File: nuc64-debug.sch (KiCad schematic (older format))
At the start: 5 parts, among them J1 SWD

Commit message: First draft for 0.2.x
Uart TX/RX have been swapped
Buttons for Reset/Boot0 have been added
Pinheader for power pins has been added
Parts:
- removed GND1, VDD1: Conn_01x01_Male, Connector_PinHeader_2.54mm:PinHeader_1x01_P2.54mm_Vertical, symbol Connector:Conn_01x01_Male
- added C1: 100n, Capacitor_SMD:C_0603_1608Metric, symbol Device:C
- added J2: POW, Connector_PinHeader_2.54mm:PinHeader_1x03_P2.54mm_Vertical, symbol Connector:Conn_01x03_Female
- added R1: 330, Resistor_SMD:R_0603_1608Metric, symbol Device:R
- added SW1: BOOT, footprints:panasonic_evpa302k, symbol Switch:SW_DIP_x01
- added SW2: RST, footprints:panasonic_evpa302k, symbol Switch:SW_DIP_x01
- DBG1: value Conn_01x10_Female -> DBG
- UART1: value Conn_01x02_Male -> UART
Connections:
- wire segments 18 -> 36
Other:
- note added: "1: ->VDD 3V3 Target\n2 :SWCLK\n3: GND\n4: SWDIO\n5: NRST\n6: SWO(reserved)\n7: Uart TX\n8: Uart RX\n9: VIN 5V\n10: BOOT0/reserved\n\nSTM32F303 does not support USB\nUse STM32F103C8 like onboard flashers\n"
- note added: "The boot-pin might be hard routed to ground.\n330 Ohms will limit current to 10mA @3V3."
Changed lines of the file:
@@
 EESchema Schematic File Version 4
-LIBS:stdebug-cache
-EELAYER 26 0
+EELAYER 30 0
 EELAYER END
 $Descr A4 11693 8268
@@
 P 4700 2600
 F 0 "DBG1" H 4594 3185 50  0000 C CNN
-F 1 "Conn_01x10_Female" H 4594 3094 50  0000 C CNN
+F 1 "DBG" H 4594 3094 50  0000 C CNN
 F 2 "footprints:Hirose_FH12-10S-0.5SH_1x10_P0.5mm_Horizontal" H 4700 2600 50  0001 C CNN
 F 3 "~" H 4700 2600 50  0001 C CNN
@@
 $EndComp
 Wire Wire Line
-	4900 2200 5700 2200
-Wire Wire Line
 	4900 2300 6800 2300
 Wire Wire Line
@@
 	6800 2500 4900 2500
 Wire Wire Line
-	4900 2600 6800 2600
+	4900 2600 5900 2600
 Wire Wire Line
 	4900 2700 6800 2700
@@
 P 6800 3200
 F 0 "UART1" H 6773 3173 50  0000 R CNN
-F 1 "Conn_01x02_Male" H 6773 3082 50  0000 R CNN
+F 1 "UART" H 6773 3082 50  0000 R CNN
 F 2 "Connector_PinSocket_2.54mm:PinSocket_1x02_P2.54mm_Vertical" H 6800 3200 50  0001 C CNN
 F 3 "~" H 6800 3200 50  0001 C CNN
@@
 	4900 2800 6300 2800
 Wire Wire Line
-	6300 2800 6300 3200
-Wire Wire Line
-	6300 3200 6600 3200
-Wire Wire Line
 	4900 2900 6100 2900
-Wire Wire Line
-	6100 2900 6100 3300
-Wire Wire Line
-	6100 3300 6600 3300
-$Comp
-L Connector:Conn_01x01_Male VDD1
-U 1 1 5BB98E93
-P 5500 2000
-F 0 "VDD1" H 5606 2178 50  0000 C CNN
-F 1 "Conn_01x01_Male" H 5606 2087 50  0000 C CNN
-F 2 "Connector_PinHeader_2.54mm:PinHeader_1x01_P2.54mm_Vertical" H 5500 2000 50  0001 C CNN
-F 3 "~" H 5500 2000 50  0001 C CNN
-	1    5500 2000
-	1    0    0    -1
-$EndComp
-$Comp
-L Connector:Conn_01x01_Male GND1
-U 1 1 5BB99075
-P 6100 2000
-F 0 "GND1" H 6206 2178 50  0000 C CNN
-F 1 "Conn_01x01_Male" H 6206 2087 50  0000 C CNN
-F 2 "Connector_PinHeader_2.54mm:PinHeader_1x01_P2.54mm_Vertical" H 6100 2000 50  0001 C CNN
-F 3 "~" H 6100 2000 50  0001 C CNN
-	1    6100 2000
-	1    0    0    -1
-$EndComp
-Wire Wire Line
-	5700 2000 5700 2200
-Connection ~ 5700 2200
-Wire Wire Line
-	5700 2200 6800 2200
-Wire Wire Line
-	6300 2000 6300 2400
-Connection ~ 6300 2400
-Wire Wire Line
-	6300 2400 6800 2400
 $Comp
 L power:GND #PWR0101
@@
 	5450 2400 5450 3300
 Connection ~ 5450 2400
-Wire Wire Line
-	5450 2400 6300 2400
+$Comp
+L Switch:SW_DIP_x01 SW2
+U 1 1 60F10269
+P 5900 4000
+F 0 "SW2" V 5854 4130 50  0000 L CNN
+F 1 "RST" V 5945 4130 50  0000 L CNN
+F 2 "footprints:panasonic_evpa302k" H 5900 4000 50  0001 C CNN
+F 3 "~" H 5900 4000 50  0001 C CNN
+	1    5900 4000
+	0    1    1    0
+$EndComp
+$Comp
+L power:GND #PWR0102
+U 1 1 60F10CF3
+P 5900 4600
+F 0 "#PWR0102" H 5900 4350 50  0001 C CNN
+F 1 "GND" H 5905 4427 50  0000 C CNN
+F 2 "" H 5900 4600 50  0001 C CNN
+F 3 "" H 5900 4600 50  0001 C CNN
+	1    5900 4600
+	1    0    0    -1
+$EndComp
+Wire Wire Line
+	5900 2600 5900 3600
+Connection ~ 5900 2600
+Wire Wire Line
+	5900 2600 6800 2600
+Wire Wire Line
+	5900 4300 5900 4400
+Wire Wire Line
+	6100 2900 6100 3200
+Wire Wire Line
+	6600 3200 6100 3200
+Wire Wire Line
+	6300 2800 6300 3300
+Wire Wire Line
+	6300 3300 6600 3300
+Text Notes 2900 3000 0    50   ~ 0
+1: ->VDD 3V3 Target\n2 :SWCLK\n3: GND\n4: SWDIO\n5: NRST\n6: SWO(reserved)\n7: Uart TX\n8: Uart RX\n9: VIN 5V\n10: BOOT0/reserved\n\nSTM32F303 does not support USB\nUse STM32F103C8 like onboard flashers\n
+$Comp
+L Switch:SW_DIP_x01 SW1
+U 1 1 60F178B4
+P 5100 4100
+F 0 "SW1" V 5054 4230 50  0000 L CNN
+F 1 "BOOT" V 5145 4230 50  0000 L CNN
+F 2 "footprints:panasonic_evpa302k" H 5100 4100 50  0001 C CNN
+F 3 "~" H 5100 4100 50  0001 C CNN
+	1    5100 4100
+	0    1    1    0
+$EndComp
+$Comp
+L power:GND #PWR0103
+U 1 1 60F178D0
+P 5100 4600
+F 0 "#PWR0103" H 5100 4350 50  0001 C CNN
+F 1 "GND" H 5105 4427 50  0000 C CNN
+F 2 "" H 5100 4600 50  0001 C CNN
+F 3 "" H 5100 4600 50  0001 C CNN
+	1    5100 4600
+	1    0    0    -1
+$EndComp
+$Comp
+L Device:R R1
+U 1 1 60F18930
+P 5100 3550
+F 0 "R1" H 5170 3596 50  0000 L CNN
+F 1 "330" H 5170 3505 50  0000 L CNN
+F 2 "Resistor_SMD:R_0603_1608Metric" V 5030 3550 50  0001 C CNN
+F 3 "~" H 5100 3550 50  0001 C CNN
+	1    5100 3550
+	1    0    0    -1
+$EndComp
+Wire Wire Line
+	4900 3100 5100 3100
+Wire Wire Line
+	5100 3100 5100 3400
+Wire Wire Line
+	5100 3700 5100 3800
+Wire Wire Line
+	5100 4600 5100 4400
+Text Notes 3150 3650 0    50   ~ 0
+The boot-pin might be hard routed to ground.\n330 Ohms will limit current to 10mA @3V3.
+$Comp
+L Connector:Conn_01x03_Female J2
+U 1 1 60F1E01B
+P 5000 1500
+F 0 "J2" H 4892 1175 50  0000 C CNN
+F 1 "POW" H 4892 1266 50  0000 C CNN
+F 2 "Connector_PinHeader_2.54mm:PinHeader_1x03_P2.54mm_Vertical" H 5000 1500 50  0001 C CNN
+F 3 "~" H 5000 1500 50  0001 C CNN
+	1    5000 1500
+	-1   0    0    1
+$EndComp
+Wire Wire Line
+	4900 2200 5750 2200
+Wire Wire Line
+	5450 2400 5600 2400
+Wire Wire Line
+	5200 1600 5600 1600
+Wire Wire Line
+	5600 1600 5600 2400
+Connection ~ 5600 2400
+Wire Wire Line
+	5600 2400 6800 2400
+Wire Wire Line
+	5200 1500 5750 1500
+Wire Wire Line
+	5750 1500 5750 2200
+Connection ~ 5750 2200
+Wire Wire Line
+	5750 2200 6800 2200
+Wire Wire Line
+	5200 1400 6000 1400
+Wire Wire Line
+	6000 1400 6000 3000
+Wire Wire Line
+	6000 3000 4900 3000
+$Comp
+L Device:C C1
+U 1 1 60F2F8B5
+P 6500 4000
+F 0 "C1" H 6615 4046 50  0000 L CNN
+F 1 "100n" H 6615 3955 50  0000 L CNN
+F 2 "Capacitor_SMD:C_0603_1608Metric" H 6538 3850 50  0001 C CNN
+F 3 "~" H 6500 4000 50  0001 C CNN
+	1    6500 4000
+	1    0    0    -1
+$EndComp
+Wire Wire Line
+	6500 3850 6500 3600
+Wire Wire Line
+	6500 3600 5900 3600
+Connection ~ 5900 3600
+Wire Wire Line
+	5900 3600 5900 3700
+Wire Wire Line
+	6500 4150 6500 4400
+Wire Wire Line
+	6500 4400 5900 4400
+Connection ~ 5900 4400
+Wire Wire Line
+	5900 4400 5900 4600
 $EndSCHEMATC

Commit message: shrink
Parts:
- added D1: LED, LED_SMD:LED_0603_1608Metric, symbol Device:LED
- added R2: R, Resistor_SMD:R_0603_1608Metric, symbol Device:R
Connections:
- net GND: now also R2.2
- net VDD: now also D1.2 (A)
- new net: D1.1 (K), R2.1
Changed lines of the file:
@@
 Connection ~ 5750 2200
 Wire Wire Line
-	5750 2200 6800 2200
+	5750 2200 6400 2200
 Wire Wire Line
 	5200 1400 6000 1400
@@
 Wire Wire Line
 	5900 4400 5900 4600
+$Comp
+L power:GND #PWR0104
+U 1 1 60F4062E
+P 8150 3650
+F 0 "#PWR0104" H 8150 3400 50  0001 C CNN
+F 1 "GND" H 8155 3477 50  0000 C CNN
+F 2 "" H 8150 3650 50  0001 C CNN
+F 3 "" H 8150 3650 50  0001 C CNN
+	1    8150 3650
+	1    0    0    -1
+$EndComp
+$Comp
+L Device:R R2
+U 1 1 60F4083F
+P 8150 3350
+F 0 "R2" H 8220 3396 50  0000 L CNN
+F 1 "R" H 8220 3305 50  0000 L CNN
+F 2 "Resistor_SMD:R_0603_1608Metric" V 8080 3350 50  0001 C CNN
+F 3 "~" H 8150 3350 50  0001 C CNN
+	1    8150 3350
+	1    0    0    -1
+$EndComp
+$Comp
+L Device:LED D1
+U 1 1 60F40F26
+P 8150 2850
+F 0 "D1" V 8189 2732 50  0000 R CNN
+F 1 "LED" V 8098 2732 50  0000 R CNN
+F 2 "LED_SMD:LED_0603_1608Metric" H 8150 2850 50  0001 C CNN
+F 3 "~" H 8150 2850 50  0001 C CNN
+	1    8150 2850
+	0    -1   -1   0
+$EndComp
+Wire Wire Line
+	8150 3650 8150 3500
+Wire Wire Line
+	8150 3200 8150 3000
+Wire Wire Line
+	6400 2200 6400 1950
+Wire Wire Line
+	6400 1950 8150 1950
+Wire Wire Line
+	8150 1950 8150 2700
+Connection ~ 6400 2200
+Wire Wire Line
+	6400 2200 6800 2200
 $EndSCHEMATC

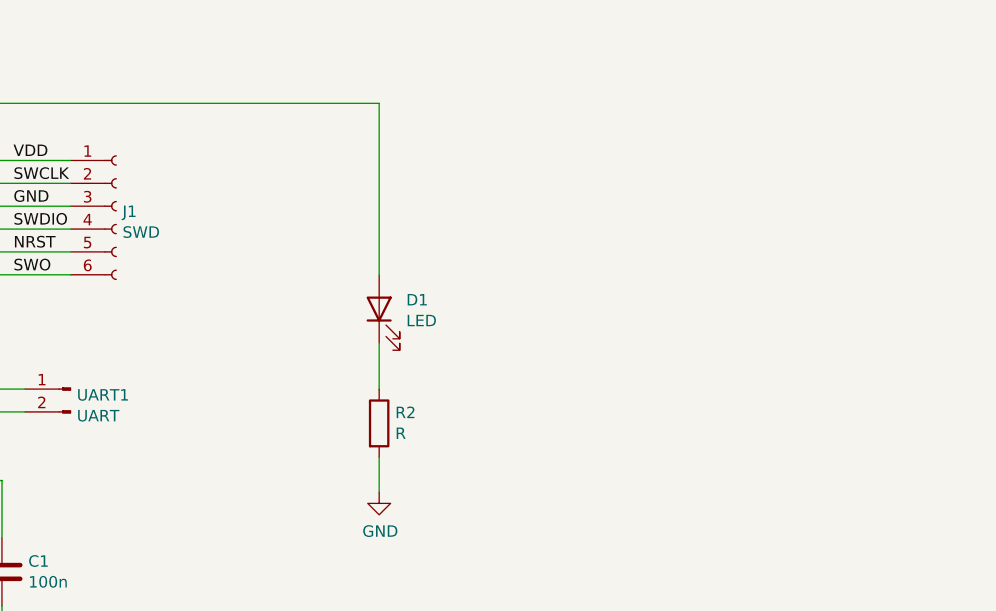
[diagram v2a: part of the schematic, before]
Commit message: [#32/#388] Boot0-button pulls high; updated symbols
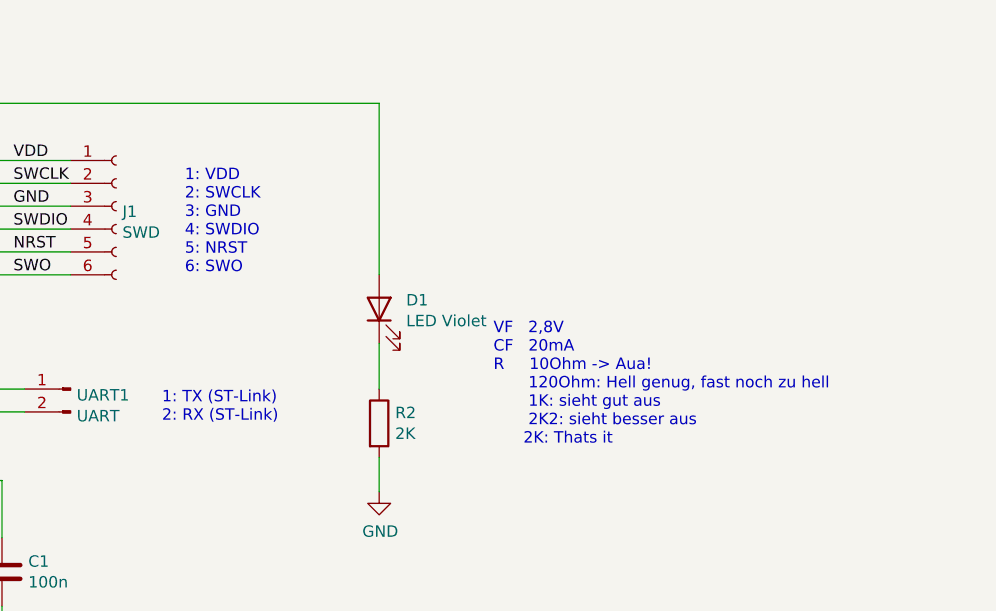
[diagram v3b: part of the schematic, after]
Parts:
- D1: value LED -> LED Violet
- R2: value R -> 2K
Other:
- note added: "1: TX (ST-Link)\n2: RX (ST-Link)"
- note added: "1: VDD\n2: SWCLK\n3: GND\n4: SWDIO\n5: NRST\n6: SWO"
- note added: "VF 2,8V\nCF 20mA\nR 10Ohm -> Aua!\n 120Ohm: Hell genug, fast noch zu hell\n 1K: sieht gut aus\n 2K2: sieht besser aus\n 2K: Thats it\n"
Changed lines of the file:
@@
 P 8150 3350
 F 0 "R2" H 8220 3396 50  0000 L CNN
-F 1 "R" H 8220 3305 50  0000 L CNN
+F 1 "2K" H 8220 3305 50  0000 L CNN
 F 2 "Resistor_SMD:R_0603_1608Metric" V 8080 3350 50  0001 C CNN
 F 3 "~" H 8150 3350 50  0001 C CNN
@@
 P 8150 2850
 F 0 "D1" V 8189 2732 50  0000 R CNN
-F 1 "LED" V 8098 2732 50  0000 R CNN
+F 1 "LED Violet" V 8098 2732 50  0000 R CNN
 F 2 "LED_SMD:LED_0603_1608Metric" H 8150 2850 50  0001 C CNN
 F 3 "~" H 8150 2850 50  0001 C CNN
@@
 Wire Wire Line
 	6400 2200 6800 2200
+Text Notes 8650 3450 0    50   ~ 0
+VF   2,8V\nCF   20mA\nR     10Ohm -> Aua!\n       120Ohm: Hell genug, fast noch zu hell\n       1K: sieht gut aus\n       2K2: sieht besser aus\n      2K: Thats it\n
+Text Notes 7300 2700 0    50   ~ 0
+1: VDD\n2: SWCLK\n3: GND\n4: SWDIO\n5: NRST\n6: SWO
+Text Notes 7200 3350 0    50   ~ 0
+1: TX (ST-Link)\n2: RX (ST-Link)
 $EndSCHEMATC
